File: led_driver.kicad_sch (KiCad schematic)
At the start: 6 parts, among them Q2 AO3400A, U3 LM358

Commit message: neat-ified schematics
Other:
- company: (none) -> The Art and Science of PCB Design
- title: (none) -> RGB LED Driver Demo Board
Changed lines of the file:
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@@
   (paper "USLetter")
   (title_block
+    (title "RGB LED Driver Demo Board")
     (date "2024-01-01")
     (rev "A01")
+    (company "The Art and Science of PCB Design")
   )
   (junction (at 99.06 71.12) (diameter 0) (color 0 0 0 0)

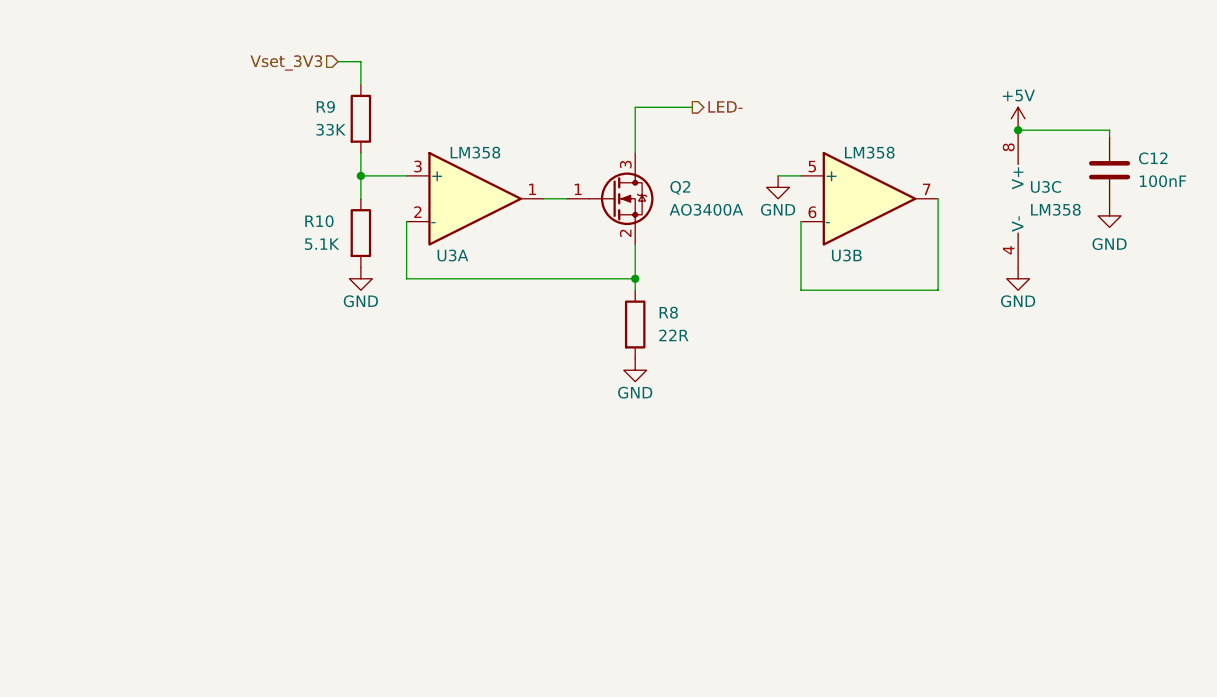
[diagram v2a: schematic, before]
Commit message: Added annotations, BOM count reduction
LED indicator resistors edited to save on BOM count

schematics made more neat, added some labels
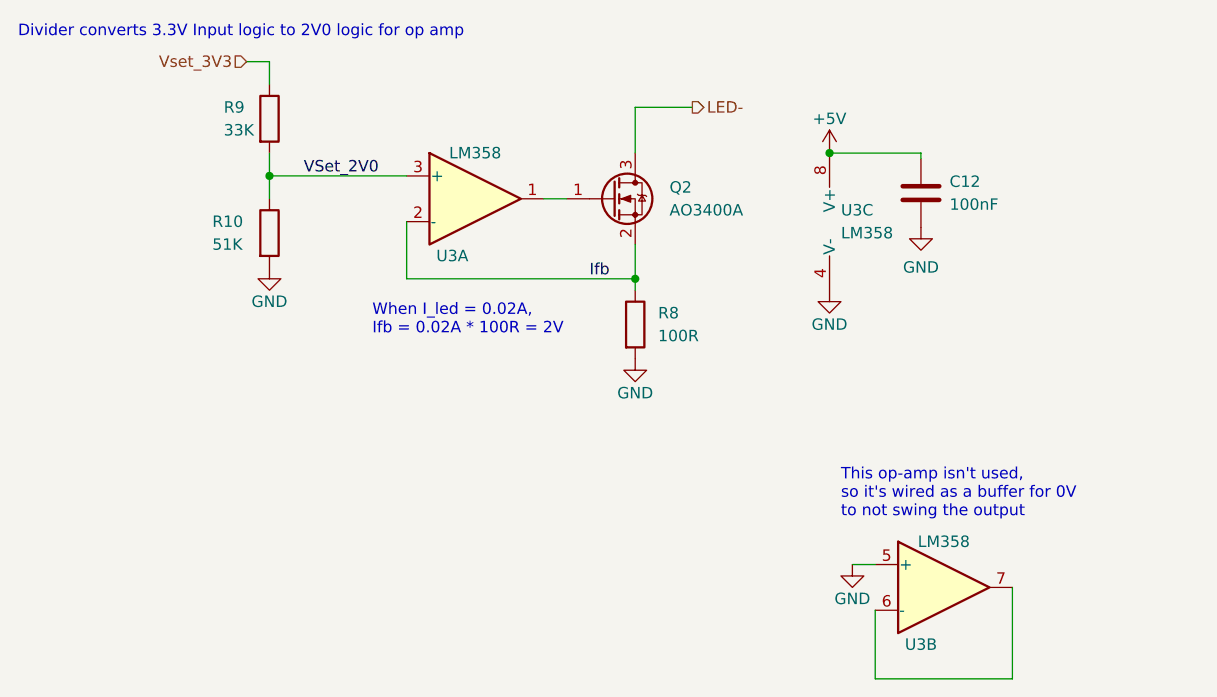
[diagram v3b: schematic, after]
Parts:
- R10: value 5.1K -> 51K
- R8: value 22R -> 100R
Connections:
- net Ifb: now reaches Q2.2 (S), R8.1, U3.2 (-)
- net VSet_2V0: now reaches R10.1, R9.2, U3.3 (+)
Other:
- note added: "Divider converts 3.3V Input logic to 2V0 logic for op amp"
- note added: "This op-amp isn't used, so it's wired as a buffer for 0V to not swing the output"
- note added: "When I_led = 0.02A, Ifb = 0.02A * 100R = 2V"
- moved on the sheet: C12, R10, R9, U3B, U3C

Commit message: added digikey PNs
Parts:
- C12: Digikey PN (none) -> 1276-1003-1-ND; MPN (none) -> CL21B104KBCNNNC
- Q2: Digikey PN (none) -> 785-1000-1-ND; MPN (none) -> AO3400A
- R10: MPN (none) -> 0805W8F5102
- R8: MPN (none) -> 0805W8F1000
- R9: MPN (none) -> 0805W8F3302
- U3: Digikey PN (none) -> 296-LM358DRCT-ND; MPN (none) -> LM358DR
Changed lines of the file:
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@@
       (effects (font (size 1.27 1.27)) hide)
     )
-    (property "Digikey PN" "" (at 153.67 76.2 0)
+    (property "Digikey PN" "296-LM358DRCT-ND" (at 153.67 76.2 0)
+      (effects (font (size 1.27 1.27)) hide)
+    )
+    (property "MPN" "LM358DR" (at 153.67 76.2 0)
       (effects (font (size 1.27 1.27)) hide)
     )
@@
       (effects (font (size 1.27 1.27)) hide)
     )
-    (property "Digikey PN" "" (at 111.76 73.66 0)
+    (property "Digikey PN" "296-LM358DRCT-ND" (at 111.76 73.66 0)
+      (effects (font (size 1.27 1.27)) hide)
+    )
+    (property "MPN" "LM358DR" (at 111.76 73.66 0)
       (effects (font (size 1.27 1.27)) hide)
     )
@@
       (effects (font (size 1.27 1.27)) (justify left) hide)
     )
-    (property "Digikey PN" "" (at 127 73.66 0)
+    (property "Digikey PN" "785-1000-1-ND" (at 127 73.66 0)
+      (effects (font (size 1.27 1.27)) hide)
+    )
+    (property "MPN" "AO3400A" (at 127 73.66 0)
       (effects (font (size 1.27 1.27)) hide)
     )
@@
     )
     (property "Digikey PN" "" (at 88.9 64.77 0)
+      (effects (font (size 1.27 1.27)) hide)
+    )
+    (property "MPN" "0805W8F3302" (at 88.9 64.77 0)
       (effects (font (size 1.27 1.27)) hide)
     )
@@
       (effects (font (size 1.27 1.27)) hide)
     )
+    (property "MPN" "0805W8F1000" (at 129.54 87.63 0)
+      (effects (font (size 1.27 1.27)) hide)
+    )
     (pin "1")
     (pin "2")
@@
     )
     (property "Digikey PN" "" (at 88.9 77.47 0)
+      (effects (font (size 1.27 1.27)) hide)
+    )
+    (property "MPN" "0805W8F5102" (at 88.9 77.47 0)
       (effects (font (size 1.27 1.27)) hide)
     )
@@
       (effects (font (size 1.27 1.27)) hide)
     )
-    (property "Digikey PN" "" (at 161.29 73.025 0)
+    (property "Digikey PN" "1276-1003-1-ND" (at 161.29 73.025 0)
+      (effects (font (size 1.27 1.27)) hide)
+    )
+    (property "MPN" "CL21B104KBCNNNC" (at 161.29 73.025 0)
       (effects (font (size 1.27 1.27)) hide)
     )
@@
       (effects (font (size 1.27 1.27)) hide)
     )
-    (property "Digikey PN" "" (at 163.83 116.84 0)
-      (effects (font (size 1.27 1.27)) hide)
-    )
+    (property "Digikey PN" "296-LM358DRCT-ND" (at 163.83 116.84 0)
+      (effects (font (size 1.27 1.27)) hide)
+    )
+    (property "MPN" "LM358DR" (at 163.83 116.84 0)
+      (effects (font (size 1.27 1.27)) hide)
+    )

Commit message: added digikey PNs to all devices
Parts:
- R10: Digikey PN (none) -> RMCF0805FT51K0CT-ND; MPN 0805W8F5102 -> RMCF0805FT51K0
- R8: Digikey PN (none) -> RMCF0805FT100RCT-ND; MPN 0805W8F1000 -> RMCF0805FT100R
- R9: Digikey PN (none) -> RMCF0805FT33K0CT-ND; MPN 0805W8F3302 -> RMCF0805FT33K0
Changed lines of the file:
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@@
       (effects (font (size 1.27 1.27)) hide)
     )
-    (property "Digikey PN" "" (at 88.9 64.77 0)
+    (property "Digikey PN" "RMCF0805FT33K0CT-ND" (at 88.9 64.77 0)
       (effects (font (size 1.27 1.27)) hide)
     )
-    (property "MPN" "0805W8F3302" (at 88.9 64.77 0)
+    (property "MPN" "RMCF0805FT33K0" (at 88.9 64.77 0)
       (effects (font (size 1.27 1.27)) hide)
     )
@@
       (effects (font (size 1.27 1.27)) hide)
     )
-    (property "Digikey PN" "" (at 129.54 87.63 0)
+    (property "Digikey PN" "RMCF0805FT100RCT-ND" (at 129.54 87.63 0)
       (effects (font (size 1.27 1.27)) hide)
     )
-    (property "MPN" "0805W8F1000" (at 129.54 87.63 0)
+    (property "MPN" "RMCF0805FT100R" (at 129.54 87.63 0)
       (effects (font (size 1.27 1.27)) hide)
     )
@@
       (effects (font (size 1.27 1.27)) hide)
     )
-    (property "Digikey PN" "" (at 88.9 77.47 0)
+    (property "Digikey PN" "RMCF0805FT51K0CT-ND" (at 88.9 77.47 0)
       (effects (font (size 1.27 1.27)) hide)
     )
-    (property "MPN" "0805W8F5102" (at 88.9 77.47 0)
+    (property "MPN" "RMCF0805FT51K0" (at 88.9 77.47 0)
       (effects (font (size 1.27 1.27)) hide)
     )

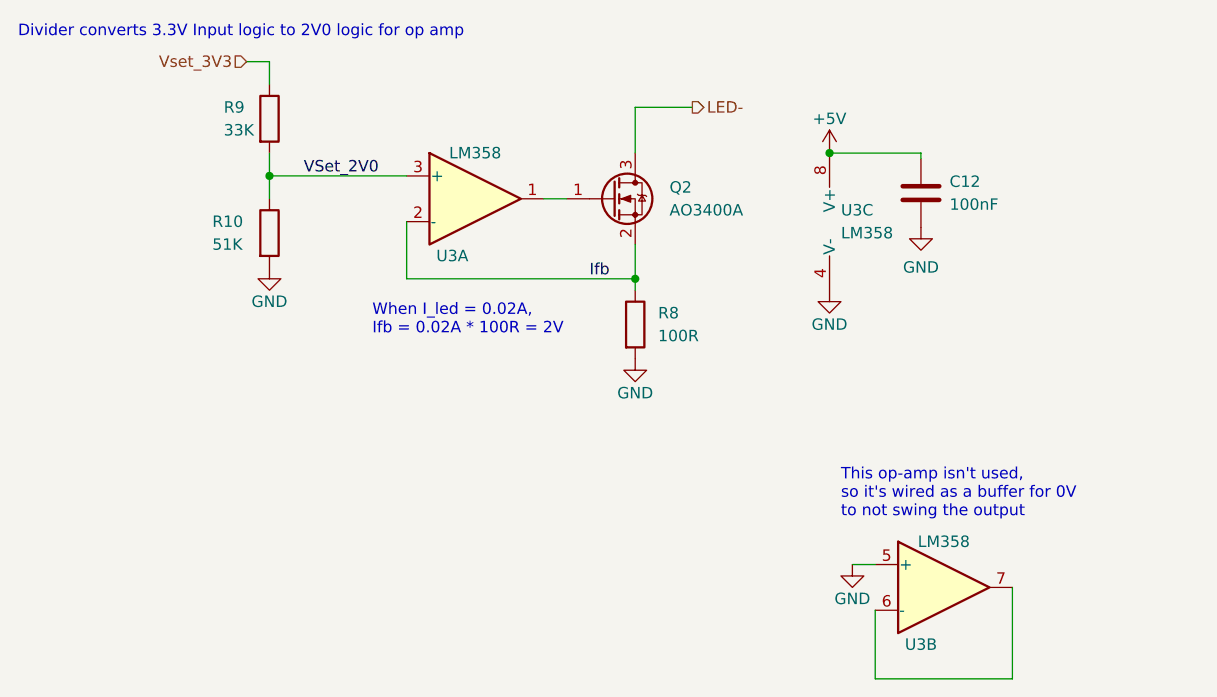
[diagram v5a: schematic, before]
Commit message: [A02] Initial release
CP2014 -> CP2012N (BOM cost reduction)
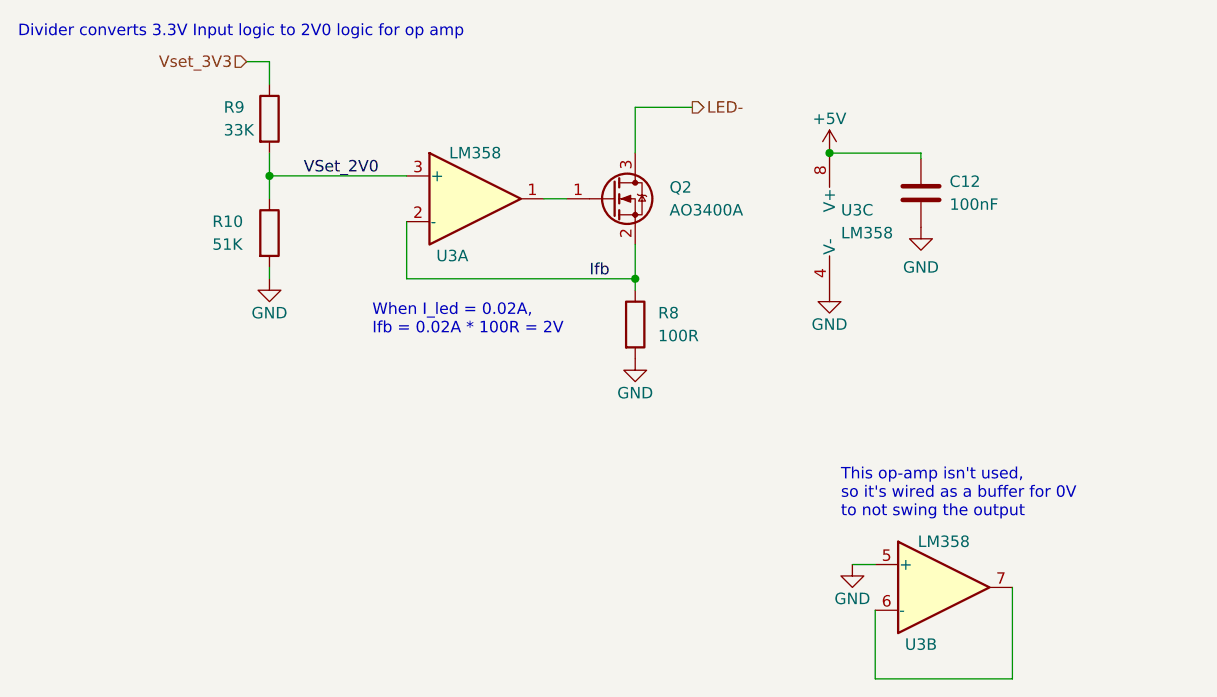
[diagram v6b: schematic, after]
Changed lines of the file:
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@@
   (title_block
     (title "RGB LED Driver Demo Board")
-    (date "2024-01-01")
-    (rev "A01")
+    (date "2024-01-02")
+    (rev "A02")
     (company "The Art and Science of PCB Design")
   )
@@
   )
   (wire (pts (xy 129.54 82.55) (xy 129.54 78.74))
+    (stroke (width 0) (type default))
+  )
+  (wire (pts (xy 88.9 82.55) (xy 88.9 81.28))
     (stroke (width 0) (type default))
   )
@@
     )
   )
-  (symbol (lib_id "power:GND") (at 88.9 81.28 0) (unit 1)
-    (in_bom yes) (on_board yes) (dnp no)
-    (property "Reference" "#PWR012" (at 88.9 87.63 0)
-      (effects (font (size 1.27 1.27)) hide)
-    )
-    (property "Value" "GND" (at 88.9 85.09 0)
-      (effects (font (size 1.27 1.27)))
-    )
-    (property "Footprint" "" (at 88.9 81.28 0)
-      (effects (font (size 1.27 1.27)) hide)
-    )
-    (property "Datasheet" "" (at 88.9 81.28 0)
-      (effects (font (size 1.27 1.27)) hide)
-    )
+  (symbol (lib_id "power:GND") (at 88.9 82.55 0) (unit 1)
+    (in_bom yes) (on_board yes) (dnp no)
+    (property "Reference" "#PWR012" (at 88.9 88.9 0)
+      (effects (font (size 1.27 1.27)) hide)
+    )
+    (property "Value" "GND" (at 88.9 86.36 0)
+      (effects (font (size 1.27 1.27)))
+    )
+    (property "Footprint" "" (at 88.9 82.55 0)
+      (effects (font (size 1.27 1.27)) hide)
+    )
+    (property "Datasheet" "" (at 88.9 82.55 0)
+      (effects (font (size 1.27 1.27)) hide)
+    )

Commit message: [A02] Edited resistor values
R11 to 51K to allow for auto reset
R3 to 270K for 34V output
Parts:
- R10: MPN RMCF0805FT51K0 -> RMCF0805FT10K0
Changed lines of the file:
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@@
       (effects (font (size 1.27 1.27)) hide)
     )
-    (property "MPN" "RMCF0805FT51K0" (at 88.9 77.47 0)
+    (property "MPN" "RMCF0805FT10K0" (at 88.9 77.47 0)
       (effects (font (size 1.27 1.27)) hide)
     )
